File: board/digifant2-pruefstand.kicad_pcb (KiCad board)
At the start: 2 copper layers, 144 x 150 mm, 78 parts, among them J0 VW ECU HARNESS, J1 12V BENCH IN, J2 IDLE VALVE N71, J3 OLED / UI I2C, Q1 2N7002, Q2 P-MOS -30V >=5A, Q3 2N7002, Q5 2N7002, SW1 PUSH, SW2 PUSH, SW3 PUSH, U1 INA226 (0x40), U2 MCP4728 (0x60), U3 INA226 (0x41), U4 AD9833, U5 Raspberry Pi Pico, U6 TS5A3159A, U7 TS5A3159A, U8 TS5A3159A, Y1 25MHz

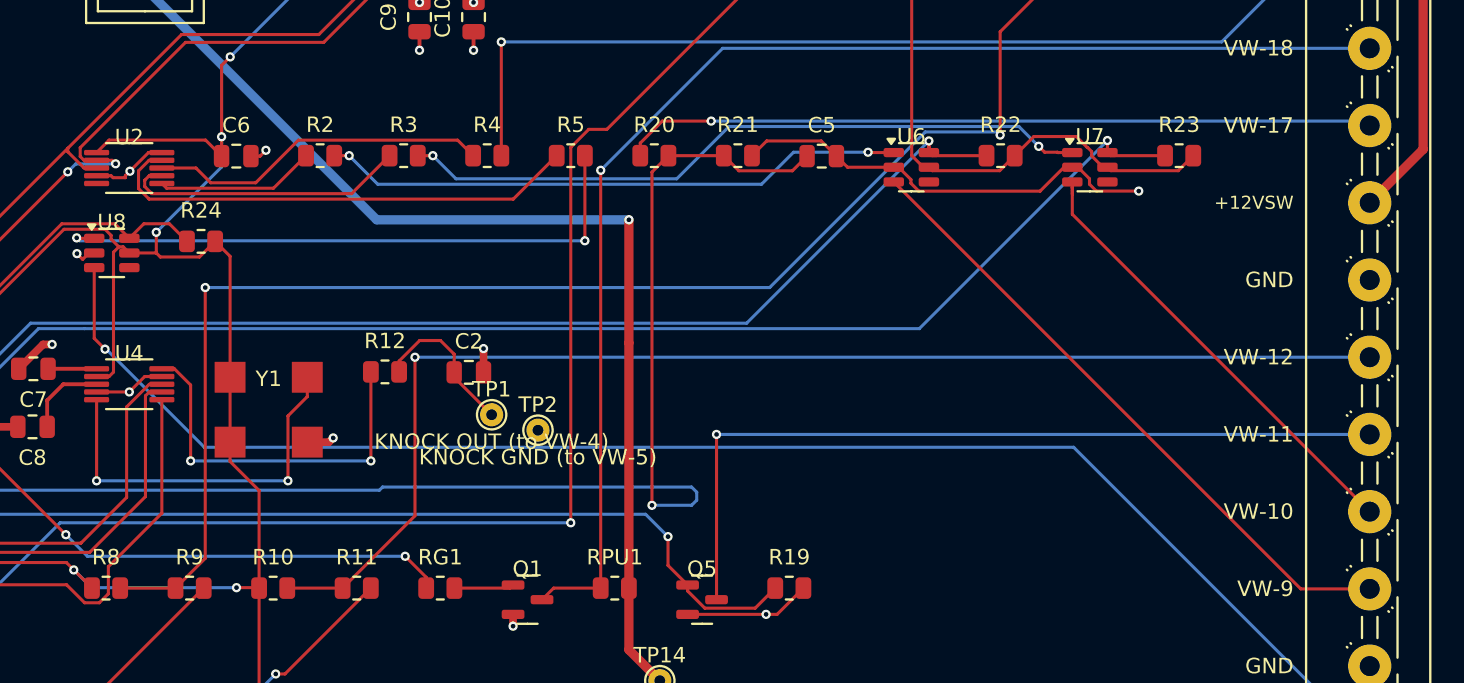
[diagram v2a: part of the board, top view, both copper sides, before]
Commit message: Apply the two bring-up fixes to the live schematic/PCB; update docs
U6/U7/U8 COM-to-NC fix and R10 = 220R, hand-edited directly in
board/*.kicad_sch and board/*.kicad_pcb (not a circuit-synth
regeneration, which would discard the hand-routing/GND pour). Verified
both ways before committing:
- ERC unchanged: same 66 warnings, same categories, 0 errors
- DRC with schematic-parity unchanged: 112 violations in the same four
  pre-existing categories, 48 schematic-parity issues, 0 unconnected
  items -- an intermediate pass surfaced one new via_dangling at U8
  pad 4 (an incomplete layer-change via from the reroute), fixed and
  reverted to the clean baseline before this commit
- U6/U7/U8 pad 4 (COM) now carries the VW net, pad 3 (NC) is open;
  R10 is 220R, still wired straight between +3V3 and VW-12

DESIGN.md and BRINGUP.md updated to say so, while keeping the bodge
instructions for the board already fabricated and in bring-up -- the
live files fix the *design*, not the physical board already printed.
Revision intentionally left as-is: more bring-up findings are still
expected before the next fab run.

Co-Authored-By: Claude Sonnet 5 <noreply@anthropic.com>
Claude-Session: https://claude.ai/code/session_01XcEuUwwCT37oProAm8HYeY
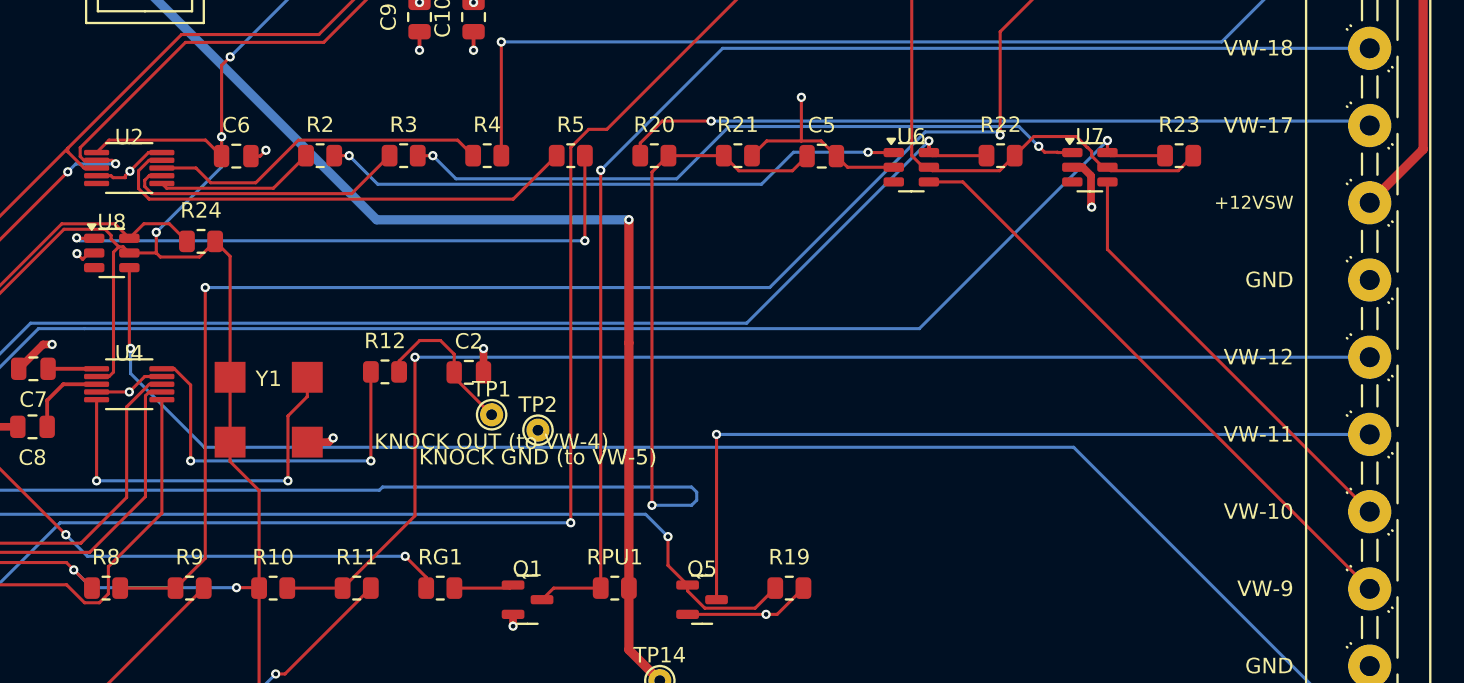
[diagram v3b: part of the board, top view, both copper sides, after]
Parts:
- R10: value 1k -> 220R
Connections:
- U6 pad 3: VW_PIN9 -> (no net)
- U6 pad 4: unconnected-(U6-Pad4-Pad4) -> VW_PIN9
- U7 pad 3: VW_PIN10 -> (no net)
- U7 pad 4: unconnected-(U7-Pad4-Pad4) -> VW_PIN10
- U8 pad 3: VW_PIN2 -> (no net)
- U8 pad 4: unconnected-(U8-Pad4-Pad4) -> VW_PIN2
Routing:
- net GND: track 135.9 -> 124.1 mm, vias 17 -> 18
- net VW_PIN9: track 41.7 -> 39.5 mm
- net VW_PIN10: track 29.8 -> 28.4 mm
- net VW_PIN2: track 98.0 -> 97.0 mm
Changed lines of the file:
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@@
 			(layers "F.Cu" "F.Mask" "F.Paste")
 			(roundrect_rratio 0.25)
-			(net "VW_PIN9")
 		)
 		(pad "4" smd roundrect
@@
 			(layers "F.Cu" "F.Mask" "F.Paste")
 			(roundrect_rratio 0.25)
-			(net "unconnected-(U6-Pad4-Pad4)")
+			(net "VW_PIN9")
 		)
 		(pad "5" smd roundrect
@@
 			)
 		)
-		(property "Value" "1k"
+		(property "Value" "220R"
 			(at 0 2 0)
 			(layer "F.Fab")
@@
 			(layers "F.Cu" "F.Mask" "F.Paste")
 			(roundrect_rratio 0.25)
-			(net "VW_PIN2")
 		)
 		(pad "4" smd roundrect
@@
 			(layers "F.Cu" "F.Mask" "F.Paste")
 			(roundrect_rratio 0.25)
-			(net "unconnected-(U8-Pad4-Pad4)")
+			(net "VW_PIN2")
 		)
 		(pad "5" smd roundrect
@@
 			(layers "F.Cu" "F.Mask" "F.Paste")
 			(roundrect_rratio 0.25)
-			(net "VW_PIN10")
 		)
 		(pad "4" smd roundrect
@@
 			(layers "F.Cu" "F.Mask" "F.Paste")
 			(roundrect_rratio 0.25)
-			(net "unconnected-(U7-Pad4-Pad4)")
+			(net "VW_PIN10")
 		)
 		(pad "5" smd roundrect
@@
 	)
 	(segment
-		(start 109.183 50.2732)
-		(end 101.33 50.2732)
+		(start 68.2325 34.275)
+		(end 68.2325 33.775)
 		(width 0.2)
 		(layer "F.Cu")
@@
 	)
 	(segment
-		(start 68.2325 34.275)
-		(end 68.2325 33.775)
+		(start 96.715 48.725)
+		(end 95.995 48.005)
 		(width 0.2)
 		(layer "F.Cu")
@@
 	)
 	(segment
-		(start 115.57 50.2674)
-		(end 112.827 50.2674)
-		(width 0.2)
-		(layer "F.Cu")
-		(net "GND")
-	)
-	(segment
 		(start 103.286 14.0367)
 		(end 103.224 14.0984)
@@
 	(segment
 		(start 91.4794 47.0231)
-		(end 95.0131 47.0231)
+		(end 93.726 47.0231)
 		(width 0.2)
 		(layer "F.Cu")
@@
 	)
 	(segment
-		(start 96.715 48.725)
-		(end 95.995 48.005)
-		(width 0.2)
+		(start 111.929999 48.725)
+		(end 112.48 49.275001)
+		(width 0.5)
 		(layer "F.Cu")
 		(net "GND")
@@
 	)
 	(segment
-		(start 49.9531 49.4013)
-		(end 49.9531 49.275)
+		(start 99.7075 48.725)
+		(end 96.715 48.725)
 		(width 0.2)
 		(layer "F.Cu")
@@
 	)
 	(segment
-		(start 110.731 48.725)
-		(end 109.183 50.2732)
+		(start 49.9531 49.4013)
+		(end 49.9531 49.275)
 		(width 0.2)
 		(layer "F.Cu")
@@
 	)
 	(segment
-		(start 100.82 49.764)
-		(end 100.82 49.5241)
-		(width 0.2)
-		(layer "F.Cu")
-		(net "GND")
-	)
-	(segment
 		(start 45.212 60.198)
 		(end 44.627 60.198)
@@
 	)
 	(segment
-		(start 99.7075 48.725)
-		(end 96.715 48.725)
-		(width 0.2)
-		(layer "F.Cu")
-		(net "GND")
-	)
-	(segment
 		(start 103.317 14.0058)
 		(end 103.333 13.9904)
@@
 	)
 	(segment
+		(start 93.726 47.0231)
+		(end 95.0131 47.0231)
+		(width 0.2)
+		(layer "F.Cu")
+		(net "GND")
+	)
+	(segment
 		(start 92.1575 77.675)
 		(end 93.8575 75.975)
@@
 	)
 	(segment
+		(start 111.2675 48.725)
+		(end 111.929999 48.725)
+		(width 0.5)
+		(layer "F.Cu")
+		(net "GND")
+	)
+	(segment
 		(start 65.4275 33.775)
 		(end 65.4275 25.7177)
@@
 	)
 	(segment
-		(start 112.827 50.2674)
-		(end 112.38 49.8212)
-		(width 0.2)
-		(layer "F.Cu")
-		(net "GND")
-	)
-	(segment
 		(start 103.333 13.9904)
 		(end 103.317 14.0058)
@@
 	)
 	(segment
+		(start 112.48 49.275001)
+		(end 112.48 51.266)
+		(width 0.5)
+		(layer "F.Cu")
+		(net "GND")
+	)
+	(segment
 		(start 103.346 13.9769)
 		(end 103.347 13.9759)
@@
 	)
 	(segment
-		(start 100.82 49.5241)
-		(end 100.021 48.725)
-		(width 0.2)
-		(layer "F.Cu")
-		(net "GND")
-	)
-	(segment
 		(start 59.62 108.21)
 		(end 57.785 108.21)
@@
 	)
 	(segment
-		(start 111.2675 48.725)
-		(end 110.731 48.725)
-		(width 0.2)
-		(layer "F.Cu")
-		(net "GND")
-	)
-	(segment
 		(start 103.344 13.9788)
 		(end 103.346 13.9769)
@@
 	)
 	(segment
-		(start 111.633 48.725)
-		(end 111.2675 48.725)
-		(width 0.2)
-		(layer "F.Cu")
-		(net "GND")
-	)
-	(segment
 		(start 79.0644 33.775)
 		(end 76.6425 33.775)
@@
 	)
 	(segment
+		(start 112.48 51.266)
+		(end 112.522 51.308)
+		(width 0.5)
+		(layer "F.Cu")
+		(net "GND")
+	)
+	(segment
 		(start 57.785 108.21)
 		(end 55.94 108.21)
@@
 	)
 	(segment
-		(start 100.021 48.725)
-		(end 99.7075 48.725)
-		(width 0.2)
-		(layer "F.Cu")
-		(net "GND")
-	)
-	(segment
-		(start 112.38 49.8212)
-		(end 112.38 49.4727)
-		(width 0.2)
-		(layer "F.Cu")
-		(net "GND")
-	)
-	(segment
 		(start 55.94 108.21)
 		(end 55.735 108.005)
@@
 	)
 	(segment
-		(start 101.33 50.2732)
-		(end 100.82 49.764)
-		(width 0.2)
-		(layer "F.Cu")
-		(net "GND")
-	)
-	(segment
-		(start 112.38 49.4727)
-		(end 111.633 48.725)
+		(start 93.726 47.0231)
+		(end 93.726 44.196)
 		(width 0.2)
 		(layer "F.Cu")
@@
 	)
 	(via
+		(at 93.726 44.196)
+		(size 0.6)
+		(drill 0.3)
+		(layers "F.Cu" "B.Cu")
+		(net "GND")
+	)
+	(via
 		(at 50.2491 48.9791)
 		(size 0.6)
@@
 	)
 	(via
-		(at 115.57 50.2674)
+		(at 112.522 51.308)
 		(size 0.6)
 		(drill 0.3)
@@
 	)
 	(segment
-		(start 130.525 76.025)
-		(end 126.058 76.025)
+		(start 104.175 49.675)
+		(end 130.525 76.025)
 		(width 0.2)
 		(layer "F.Cu")
@@
 	)
 	(segment
-		(start 126.058 76.025)
-		(end 99.7075 49.675)
+		(start 101.9825 49.675)
+		(end 104.175 49.675)
 		(width 0.2)
 		(layer "F.Cu")
@@
 	)
 	(segment
-		(start 47.9375 59.8046)
-		(end 48.6371 60.5042)
+		(start 50.2125 60.3725)
+		(end 50.2125 55.225)
 		(width 0.2)
 		(layer "F.Cu")
@@
 	)
 	(segment
-		(start 47.9375 55.225)
-		(end 47.9375 59.8046)
+		(start 50.292 60.452)
+		(end 50.2125 60.3725)
 		(width 0.2)
 		(layer "F.Cu")
@@
 	)
 	(via
-		(at 48.6371 60.5042)
+		(at 50.292 60.452)
 		(size 0.6)
 		(drill 0.3)
@@
 	)
 	(segment
-		(start 48.6371 60.5042)
-		(end 48.7158 60.5042)
+		(start 55.0684 66.8568)
+		(end 50.292 62.0804)
 		(width 0.2)
 		(layer "B.Cu")
@@
 	)
 	(segment
-		(start 48.7158 60.5042)
-		(end 55.0684 66.8568)
-		(width 0.2)
-		(layer "B.Cu")
-		(net "VW_PIN2")
-	)
-	(segment
 		(start 111.357 66.8568)
 		(end 130.525 86.025)
@@
 	)
 	(segment
-		(start 111.268 50.4596)
-		(end 111.268 50.1981)
+		(start 50.292 62.0804)
+		(end 50.292 60.452)
 		(width 0.2)
-		(layer "F.Cu")
-		(net "VW_PIN10")
-	)
-	(segment
-		(start 111.268 50.0668)
-		(end 111.268 49.9365)
-		(width 0.2)
-		(layer "F.Cu")
-		(net "VW_PIN10")
-	)
-	(segment
-		(start 111.268 49.9365)
-		(end 111.268 49.8057)
-		(width 0.2)
-		(layer "F.Cu")
-		(net "VW_PIN10")
-	)
-	(segment
-		(start 111.268 50.0673)
-		(end 111.268 50.0668)
-		(width 0.2)
-		(layer "F.Cu")
-		(net "VW_PIN10")
-	)
-	(segment
-		(start 111.268 49.8057)
-		(end 111.2675 49.8052)
-		(width 0.2)
-		(layer "F.Cu")
-		(net "VW_PIN10")
-	)
-	(segment
-		(start 111.268 50.0673)
-		(end 111.268 50.0668)
-		(width 0.2)
-		(layer "F.Cu")
-		(net "VW_PIN10")
-	)
-	(segment
-		(start 130.525 71.025)
-		(end 111.268 51.7675)
-		(width 0.2)
-		(layer "F.Cu")
-		(net "VW_PIN10")
-	)
-	(segment
-		(start 111.268 49.8057)
-		(end 111.268 49.675)
-		(width 0.2)
-		(layer "F.Cu")
-		(net "VW_PIN10")
-	)
-	(segment
-		(start 111.2675 49.8052)
-		(end 111.2675 49.675)
-		(width 0.2)
-		(layer "F.Cu")
-		(net "VW_PIN10")
-	)
-	(segment
-		(start 111.268 50.4596)
-		(end 111.268 50.1981)
-		(width 0.2)
-		(layer "F.Cu")
-		(net "VW_PIN10")
-	)
-	(segment
-		(start 111.268 50.1981)
-		(end 111.268 50.0673)
-		(width 0.2)
-		(layer "F.Cu")
-		(net "VW_PIN10")
+		(layer "B.Cu")
+		(net "VW_PIN2")
 	)
 	(segment
-		(start 111.268 51.7675)
-		(end 111.268 50.4596)
+		(start 113.5425 54.0425)
+		(end 130.525 71.025)
 		(width 0.2)
 		(layer "F.Cu")
@@
 	)
 	(segment
-		(start 111.268 50.0668)
-		(end 111.268 49.9365)
+		(start 113.5425 49.675)
+		(end 113.5425 54.0425)
 		(width 0.2)
 		(layer "F.Cu")

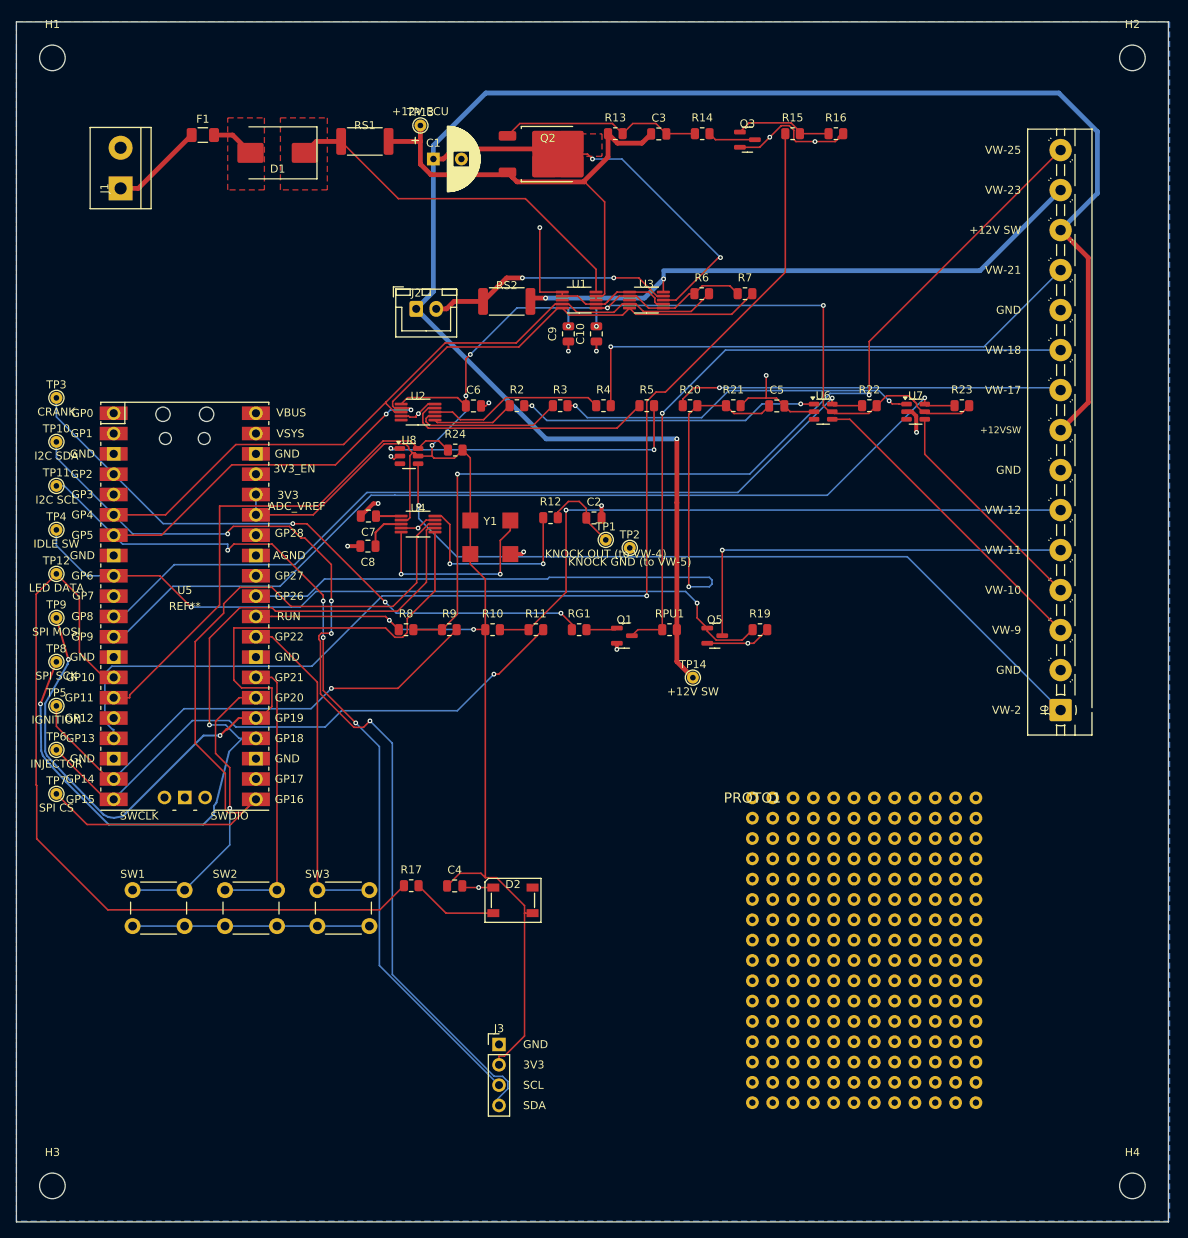
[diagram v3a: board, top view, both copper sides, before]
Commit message: PCB: Kelvin-route U1's IN-/VBUS sense to RS1 pad 2; document the U3 flaw
Hand-edited layout: U1 pins 8/9 now run on their own 0.2 mm trace to RS1
pad 2, alongside the IN+ trace, replacing the tap ~29 mm downstream on the
power trace that made U1 read 48 % high. Also moved C9 (next to C10 by U3)
and TP14 (2 mm), re-routed a few nets around the new trace, removed a
dangling +3V3 stub. DRC with the project rules: 112 violations, the same
as before (0 new), 0 unconnected.

DESIGN.md: U1 layout fixed (firmware workaround stays for the built board);
U3's IN+ sense taps the return trace 17.8 mm downstream of RS2, so expect
valve_a ~20-45 % high; fix is its own trace from RS2 pad 2. BRINGUP.md
notes the U3 prediction for Stage 5.

Co-Authored-By: Claude Sonnet 5.5 <noreply@anthropic.com>
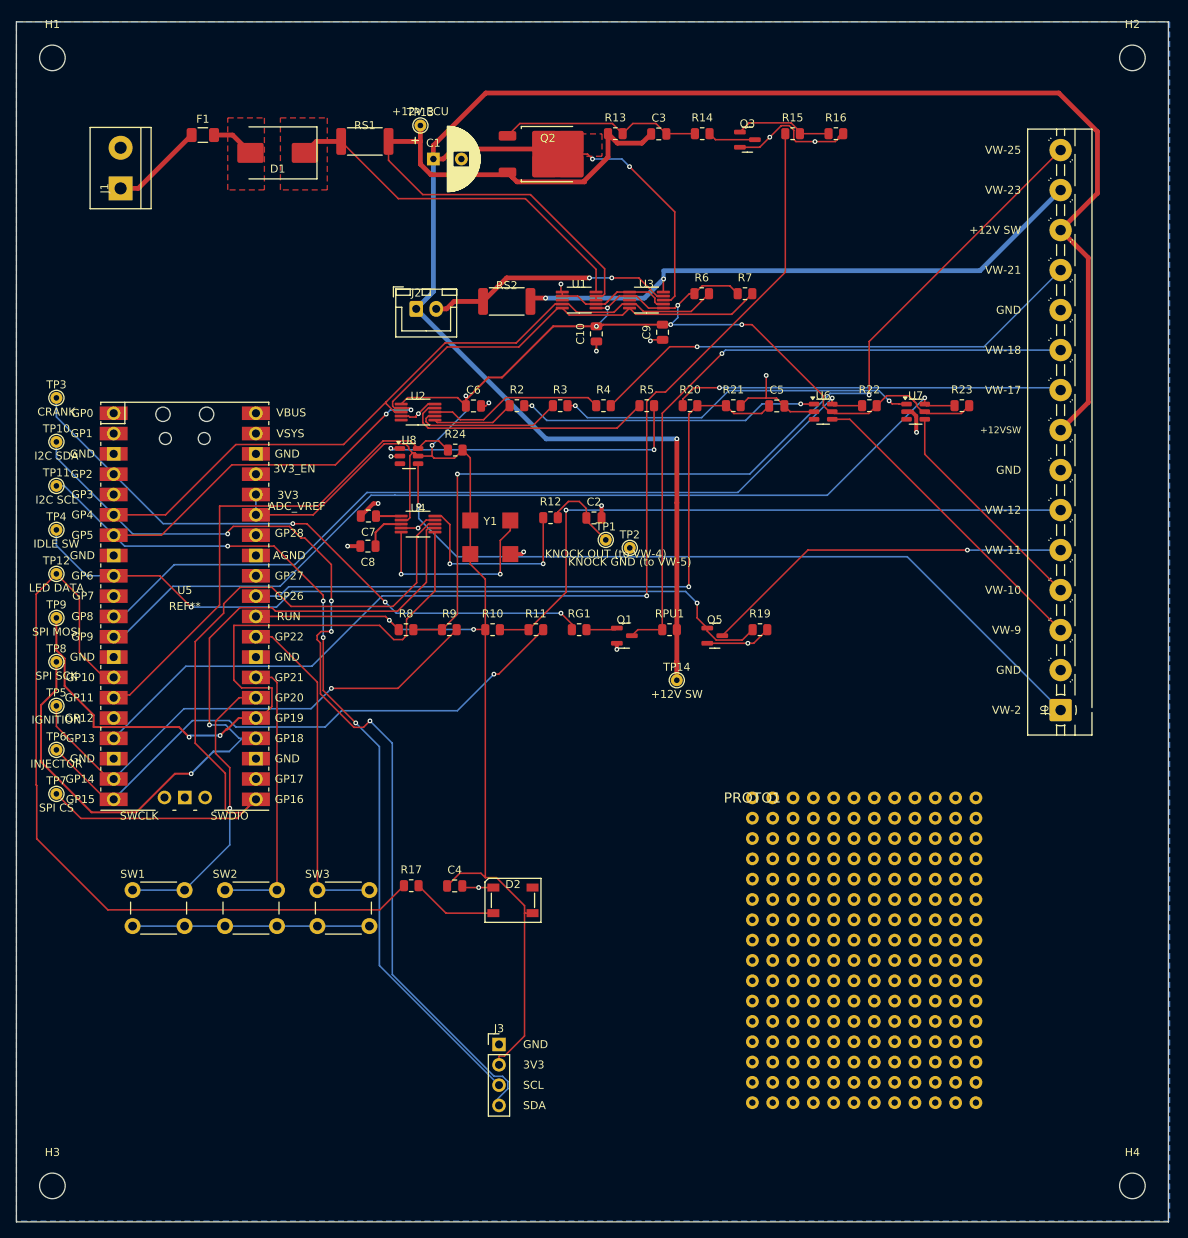
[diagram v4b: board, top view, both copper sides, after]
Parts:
- moved C9 11.8 mm to (80.8, 38.8)
- moved TP14 2.04 mm to (82.5, 82.3)
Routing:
- net +12V_ECU: track 61.1 -> 84.2 mm
- net GP19_SPI_MOSI: track 105.7 -> 91.2 mm
- net GND: track 124.1 -> 114.5 mm
- net +3V3: track 293.2 -> 283.9 mm
- net GP26_AFM_REF_ADC: track 94.5 -> 87.5 mm
- net GP13_ECU_PWR_EN: track 146.1 -> 139.6 mm
- net VW_PIN11: track 53.0 -> 46.7 mm
- net +12V_ECU_SW: track 280.6 -> 274.9 mm
- net VW_PIN21: track 67.6 -> 63.2 mm
- net GP18_SPI_SCK: track 105.3 -> 102.0 mm
- net I2C_SCL: track 209.0 -> 208.0 mm
- net GP16_SPI_CS: track 97.2 -> 96.6 mm
